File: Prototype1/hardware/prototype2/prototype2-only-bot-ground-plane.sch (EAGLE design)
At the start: 94 parts, among them IC1 ATTINY13A-SSU, IC2 LDL112D33R, IC3 FT2232HL-REEL, IC4 93LC46BT-I_OT, IC5 APA104, IC6 APA104, IC7 APA104, IC8 APA104, J4 DN PAIR, U2 ESP-WROOM-32

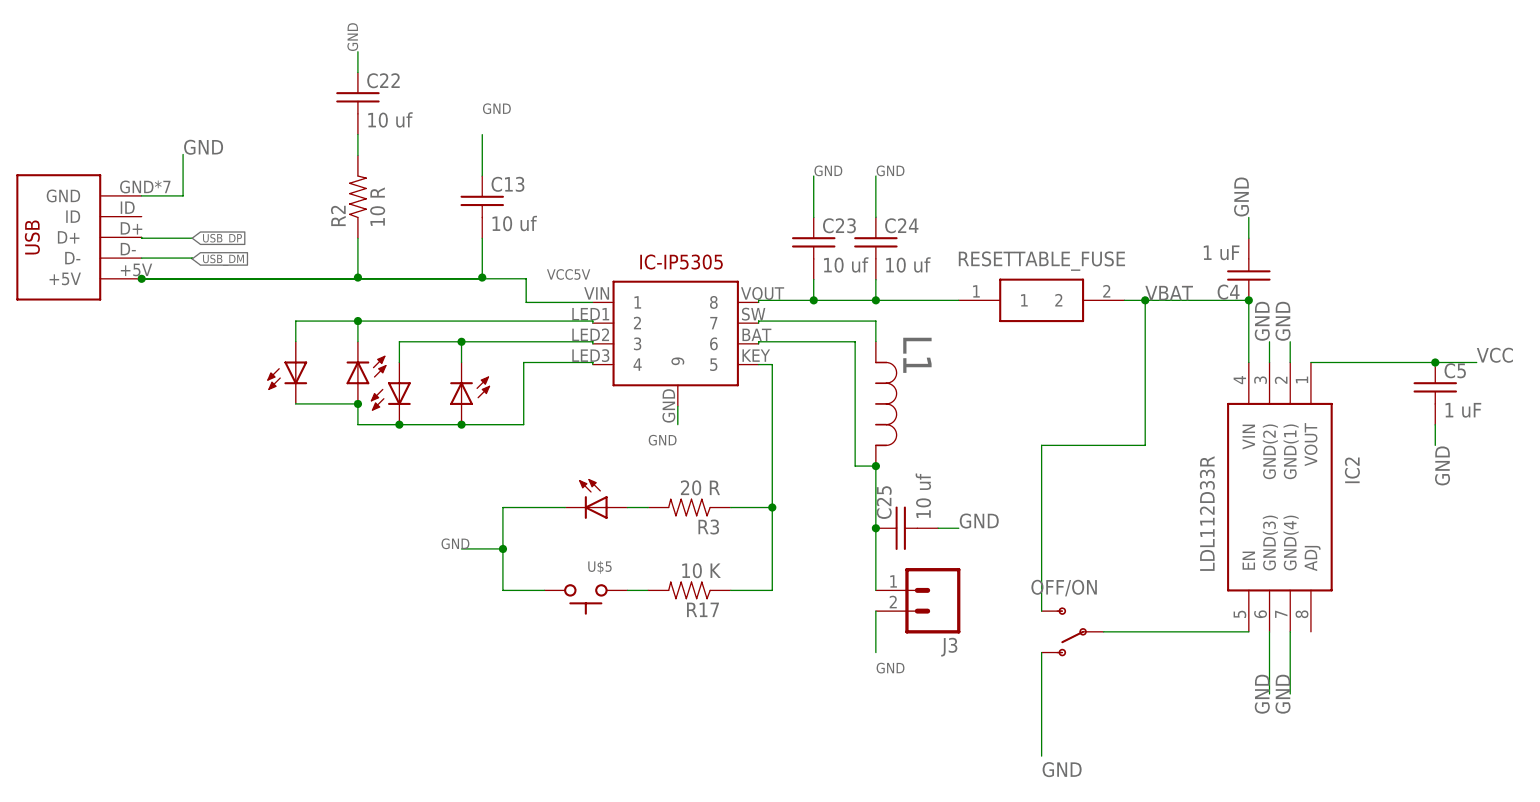
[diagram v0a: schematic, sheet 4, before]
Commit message: increased width of traces and tried a different package for slide switch
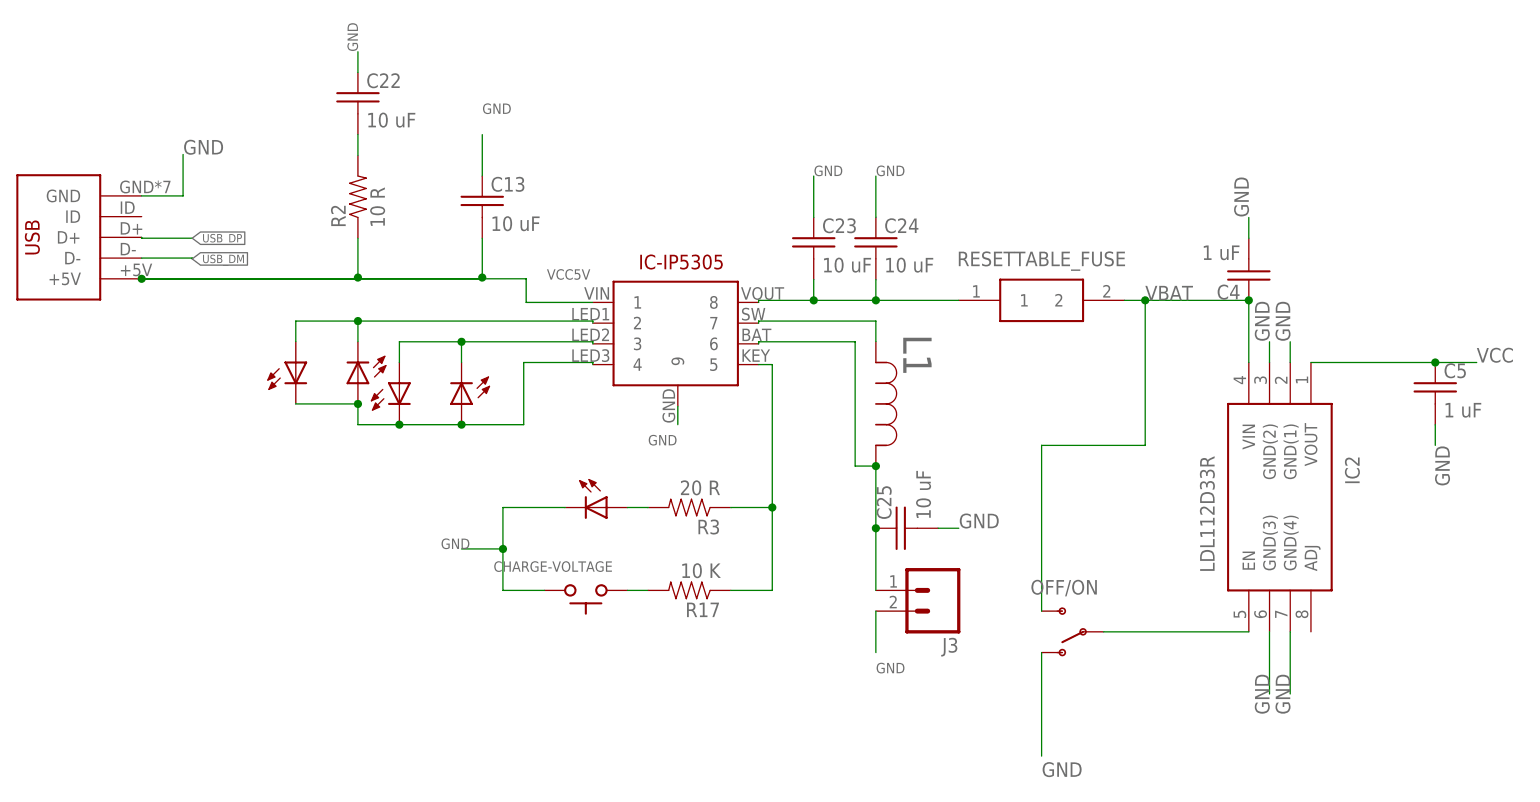
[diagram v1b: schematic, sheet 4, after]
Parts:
- C1, C13, C22, C23, C24, C25: value 10 uf -> 10 uF
- CHARGE-VOLTAGE: value SWITCH_TACTILETACTILE-2PIN-NARROW -> UserButton
- OFF/ON: device switches:SWITCH-SPSTPTH -> switches:SWITCH-SPSTPTH_LOCK
- R10: value 2.2K -> 2.2 K
- R11, R12: value 56 -> 56 R
- R22: value 4.7K -> 4.7 K
- R5: value 1K -> 1 K
- renumbered U$5 to CHARGE-VOLTAGE
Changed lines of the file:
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@@
 <part name="R1" library="dc-26" deviceset="RESISTOR" device="0805-RES" value="10K"/>
 <part name="R4" library="dc-26" deviceset="RESISTOR" device="0805-RES" value="10K"/>
-<part name="C1" library="passives" deviceset="C-US" device="C0805" value="10 uf"/>
+<part name="C1" library="passives" deviceset="C-US" device="C0805" value="10 uF"/>
 <part name="U$2" library="connector" deviceset="DX4R005JJ2" device="DX4R005JJ2"/>
 <part name="RESETTABLE_FUSE" library="passives" deviceset="0ZCJ0050FF2G" device=""/>
@@
 <part name="C11" library="passives" deviceset="C-US" device="C0805" value="0.1 uF"/>
 <part name="C12" library="passives" deviceset="C-US" device="C0805" value="0.1 uF"/>
-<part name="R5" library="passives" deviceset="RESISTOR" device="0805-RES" value="1K"/>
+<part name="R5" library="passives" deviceset="RESISTOR" device="0805-RES" value="1 K"/>
 <part name="R6" library="passives" deviceset="RESISTOR" device="0805-RES" value="10 K"/>
 <part name="C14" library="passives" deviceset="C-US" device="C0805" value="0.1 uF"/>
@@
 <part name="IC4" library="eeprom" deviceset="93LC46BT-I_OT" device=""/>
 <part name="R9" library="passives" deviceset="RESISTOR" device="0805-RES" value="10K"/>
-<part name="R10" library="passives" deviceset="RESISTOR" device="0805-RES" value="2.2K"/>
+<part name="R10" library="passives" deviceset="RESISTOR" device="0805-RES" value="2.2 K"/>
 <part name="LED2" library="leds" deviceset="LED" device="3MM" value="rx-led"/>
 <part name="LED3" library="leds" deviceset="LED" device="3MM" value="tx-led"/>
-<part name="R11" library="passives" deviceset="RESISTOR" device="0805-RES" value="56"/>
-<part name="R12" library="passives" deviceset="RESISTOR" device="0805-RES" value="56"/>
+<part name="R11" library="passives" deviceset="RESISTOR" device="0805-RES" value="56 R"/>
+<part name="R12" library="passives" deviceset="RESISTOR" device="0805-RES" value="56 R"/>
 <part name="EMIFILTER1" library="passives" deviceset="MEM2012S101RT" device=""/>
 <part name="EMIFILTER2" library="passives" deviceset="MEM2012S101RT" device=""/>
 <part name="D1" library="passives" deviceset="DIODE" device="SMA"/>
-<part name="R22" library="passives" deviceset="RESISTOR" device="0805-RES" value="4.7K"/>
+<part name="R22" library="passives" deviceset="RESISTOR" device="0805-RES" value="4.7 K"/>
 <part name="R23" library="passives" deviceset="RESISTOR" device="0805-RES" value="10 K"/>
 <part name="R24" library="passives" deviceset="RESISTOR" device="0805-RES" value="10 K"/>
@@
 <part name="C3" library="passives" deviceset="C-US" device="C0805" value="0.1 uF"/>
 <part name="U$4" library="defcon" deviceset="DC-27-SAO" device=""/>
-<part name="OFF/ON" library="switches" deviceset="SWITCH-SPST" device="PTH"/>
+<part name="OFF/ON" library="switches" deviceset="SWITCH-SPST" device="PTH_LOCK"/>
 <part name="IC-IP5305" library="charging-ic" deviceset="IP5305" device="ESOP8" package3d_urn="urn:adsk.eagle:package:8974512/1"/>
 <part name="LED1" library="leds" deviceset="LED" device="3MM"/>
@@
 <part name="LED5" library="leds" deviceset="LED" device="3MM"/>
 <part name="LED6" library="leds" deviceset="LED" device="3MM"/>
-<part name="C13" library="passives" deviceset="C-US" device="C0805" value="10 uf"/>
-<part name="C22" library="passives" deviceset="C-US" device="C0805" value="10 uf"/>
-<part name="C23" library="passives" deviceset="C-US" device="C0805" value="10 uf"/>
-<part name="C24" library="passives" deviceset="C-US" device="C0805" value="10 uf"/>
+<part name="C13" library="passives" deviceset="C-US" device="C0805" value="10 uF"/>
+<part name="C22" library="passives" deviceset="C-US" device="C0805" value="10 uF"/>
+<part name="C23" library="passives" deviceset="C-US" device="C0805" value="10 uF"/>
+<part name="C24" library="passives" deviceset="C-US" device="C0805" value="10 uF"/>
 <part name="R2" library="passives" deviceset="RESISTOR" device="0805-RES" value="10 R"/>
 <part name="J3" library="connector" deviceset="M02" device="PTH"/>
@@
 <part name="R3" library="passives" deviceset="RESISTOR" device="0805-RES" value="20 R"/>
 <part name="R17" library="passives" deviceset="RESISTOR" device="0805-RES" value="10 K"/>
-<part name="C25" library="passives" deviceset="C-US" device="C0805" value="10 uf"/>
+<part name="C25" library="passives" deviceset="C-US" device="C0805" value="10 uF"/>
 <part name="LED7" library="leds" deviceset="LED" device="3MM"/>
-<part name="U$5" library="switches" deviceset="SWITCH_TACTILE" device="TACTILE-2PIN-NARROW"/>
+<part name="CHARGE-VOLTAGE" library="switches" deviceset="SWITCH_TACTILE" device="TACTILE-2PIN-NARROW" value="UserButton"/>
 <part name="J2" library="connector" deviceset="M06" device="SILK_FEMALE_PTH"/>
 <part name="IC1" library="ICs" deviceset="ATTINY13A-SSU" device=""/>
@@
 <attribute name="VALUE" x="66.548" y="47.625" size="1.778" layer="96"/>
 </instance>
-<instance part="U$5" gate="G$1" x="68.58" y="43.18" smashed="yes" rot="R90">
+<instance part="CHARGE-VOLTAGE" gate="G$1" x="68.58" y="43.18" smashed="yes" rot="R90">
 <attribute name="NAME" x="71.882" y="46.736" size="1.27" layer="95" font="vector" rot="R180"/>
 </instance>
@@
 <wire x1="66.04" y1="53.34" x2="58.42" y2="53.34" width="0.1524" layer="91"/>
 <wire x1="58.42" y1="53.34" x2="58.42" y2="48.26" width="0.1524" layer="91"/>
-<pinref part="U$5" gate="G$1" pin="A"/>
+<pinref part="CHARGE-VOLTAGE" gate="G$1" pin="A"/>
 <wire x1="58.42" y1="48.26" x2="58.42" y2="43.18" width="0.1524" layer="91"/>
 <wire x1="58.42" y1="43.18" x2="63.5" y2="43.18" width="0.1524" layer="91"/>
@@
 <segment>
 <pinref part="R17" gate="G$1" pin="2"/>
-<pinref part="U$5" gate="G$1" pin="C"/>
+<pinref part="CHARGE-VOLTAGE" gate="G$1" pin="C"/>
 <wire x1="76.2" y1="43.18" x2="73.66" y2="43.18" width="0.1524" layer="91"/>
 </segment>

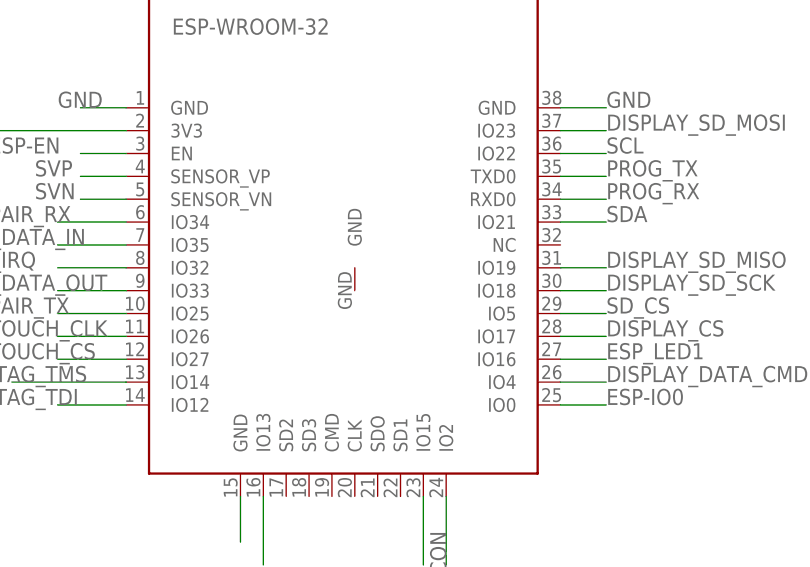
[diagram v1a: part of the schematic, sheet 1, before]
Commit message: fixed bug with center ground plane on esp32
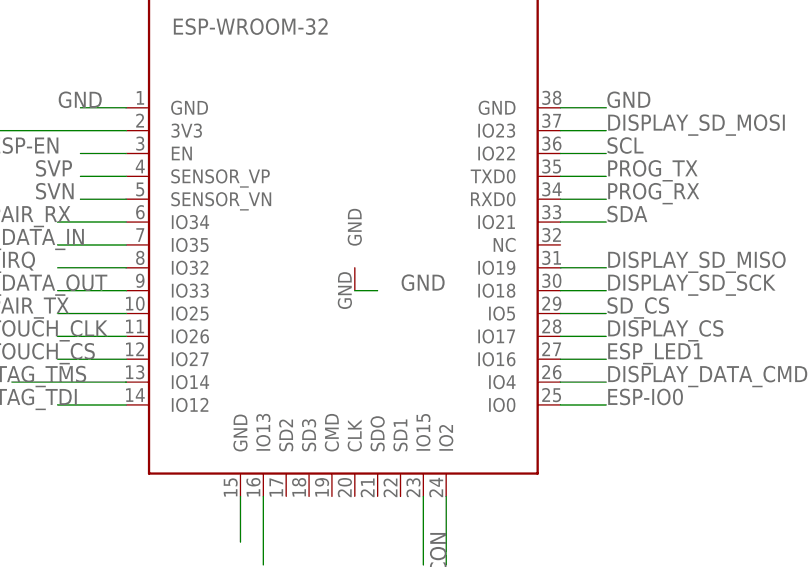
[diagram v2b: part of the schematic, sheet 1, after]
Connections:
- net GND: now also U2.GND
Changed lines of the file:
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@@
 <label x="195.58" y="71.12" size="1.778" layer="95"/>
+</segment>
+<segment>
+<pinref part="U2" gate="G$1" pin="GND"/>
+<wire x1="81.28" y1="38.1" x2="83.82" y2="38.1" width="0.1524" layer="91"/>
+<label x="86.36" y="38.1" size="1.778" layer="95"/>
 </segment>
 </net>

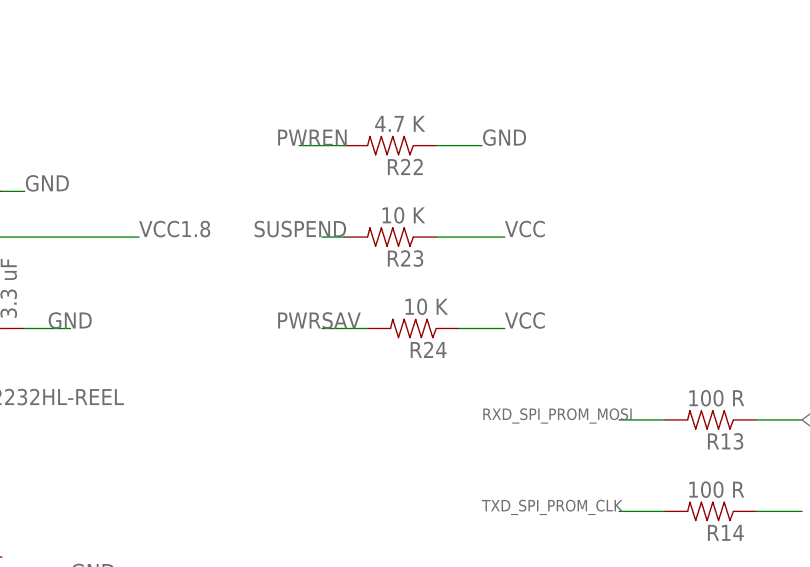
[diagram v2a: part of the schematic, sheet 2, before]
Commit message: removed inputs to output pins....duh
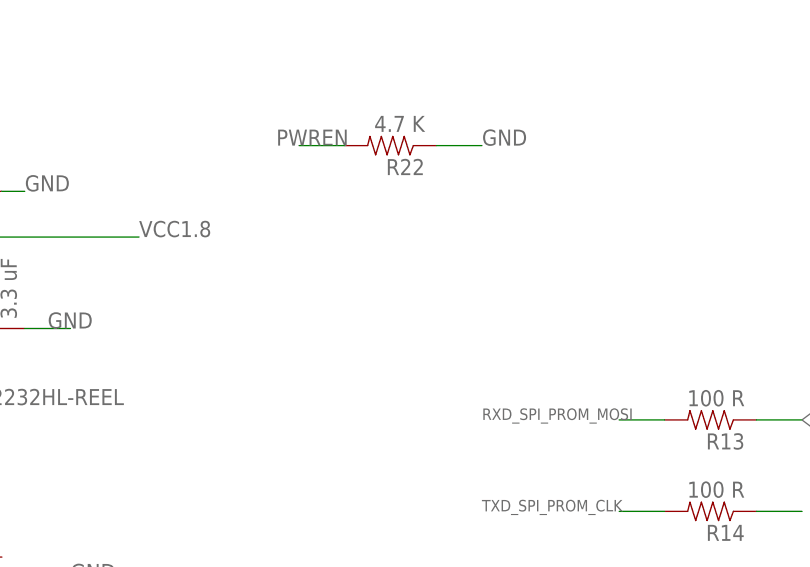
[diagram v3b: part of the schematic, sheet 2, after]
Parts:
- removed R23, R24: 10 K, passives:RESISTOR0805-RES
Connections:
- net PWRSAV: no longer R24.2
- net SUSPEND: no longer R23.2
- net VCC: no longer R23.1, R24.1
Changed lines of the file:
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@@
 <part name="D1" library="passives" deviceset="DIODE" device="SMA"/>
 <part name="R22" library="passives" deviceset="RESISTOR" device="0805-RES" value="4.7 K"/>
-<part name="R23" library="passives" deviceset="RESISTOR" device="0805-RES" value="10 K"/>
-<part name="R24" library="passives" deviceset="RESISTOR" device="0805-RES" value="10 K"/>
 <part name="J8" library="connector" deviceset="M06" device="NO_SILK_YES_STOP"/>
 <part name="J1" library="connector" deviceset="M14" device=""/>
@@
 <attribute name="VALUE" x="130.81" y="115.062" size="1.778" layer="96" rot="R180"/>
 </instance>
-<instance part="R23" gate="G$1" x="127" y="101.6" smashed="yes" rot="R180">
-<attribute name="NAME" x="130.81" y="100.1014" size="1.778" layer="95" rot="R180"/>
-<attribute name="VALUE" x="130.81" y="104.902" size="1.778" layer="96" rot="R180"/>
-</instance>
-<instance part="R24" gate="G$1" x="129.54" y="91.44" smashed="yes" rot="R180">
-<attribute name="NAME" x="133.35" y="89.9414" size="1.778" layer="95" rot="R180"/>
-<attribute name="VALUE" x="133.35" y="94.742" size="1.778" layer="96" rot="R180"/>
-</instance>
 <instance part="C3" gate="G$1" x="22.86" y="149.86" smashed="yes" rot="R270">
 <attribute name="NAME" x="23.495" y="156.464" size="1.778" layer="95" rot="R270"/>
@@
 <wire x1="-73.66" y1="27.94" x2="-83.82" y2="27.94" width="0.1524" layer="91"/>
 <label x="-83.82" y="27.94" size="1.778" layer="95"/>
-</segment>
-<segment>
-<pinref part="R23" gate="G$1" pin="1"/>
-<wire x1="132.08" y1="101.6" x2="139.7" y2="101.6" width="0.1524" layer="91"/>
-<label x="139.7" y="101.6" size="1.778" layer="95"/>
-</segment>
-<segment>
-<pinref part="R24" gate="G$1" pin="1"/>
-<wire x1="134.62" y1="91.44" x2="139.7" y2="91.44" width="0.1524" layer="91"/>
-<label x="139.7" y="91.44" size="1.778" layer="95"/>
 </segment>
 <segment>
@@
 <label x="91.44" y="35.56" size="1.778" layer="95"/>
 </segment>
-<segment>
-<pinref part="R23" gate="G$1" pin="2"/>
-<wire x1="121.92" y1="101.6" x2="119.38" y2="101.6" width="0.1524" layer="91"/>
-<label x="111.76" y="101.6" size="1.778" layer="95"/>
-</segment>
 </net>
 <net name="PWRSAV" class="0">
@@
 <label x="50.8" y="88.9" size="1.778" layer="95" rot="R90"/>
 </segment>
-<segment>
-<pinref part="R24" gate="G$1" pin="2"/>
-<wire x1="124.46" y1="91.44" x2="119.38" y2="91.44" width="0.1524" layer="91"/>
-<label x="114.3" y="91.44" size="1.778" layer="95"/>
-</segment>
-</net>
+</net>
